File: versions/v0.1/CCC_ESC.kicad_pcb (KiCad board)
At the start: 4 copper layers, 100 x 65 mm, 158 parts, among them J1 Conn_01x04, J2 Conn_01x06, J3 Conn_01x06, J4 Conn_01x06, U1 NCP5183, U2 NCP5183, U3 NCP5183, U4 NCS20074D, U5 STM32F401CCU6_Balckpill, U6 PQDE6W-Q110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

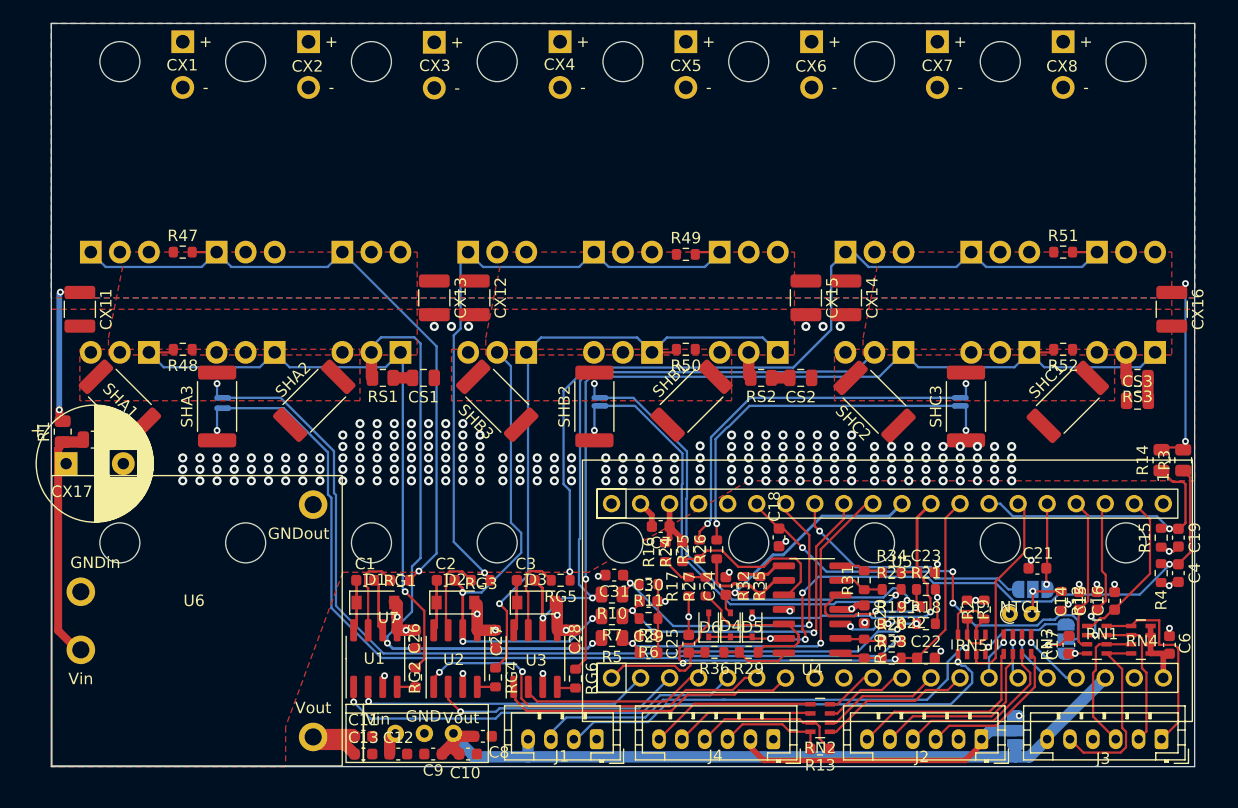
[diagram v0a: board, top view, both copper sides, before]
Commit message: finished power and gnd planes and pours
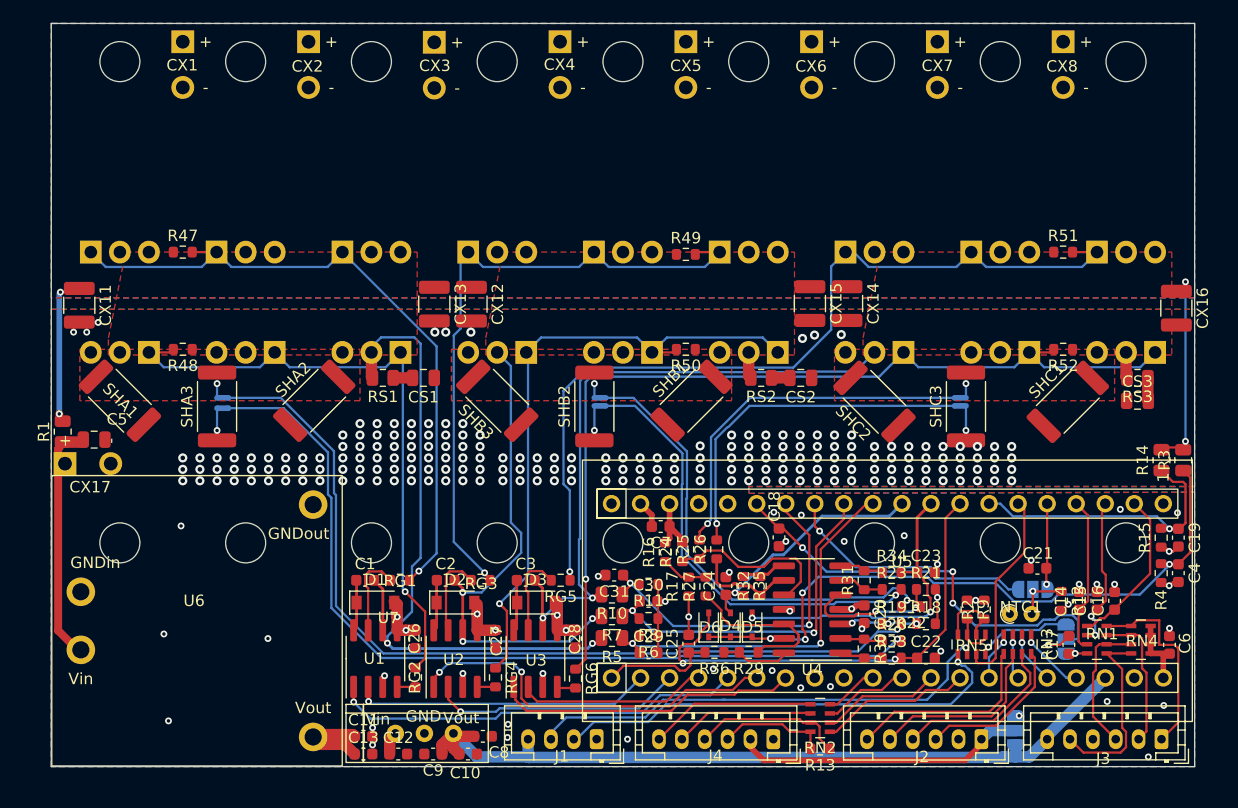
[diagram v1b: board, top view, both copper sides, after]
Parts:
- CX17: footprint Capacitor_THT:CP_Radial_D10.0mm_P5.00mm -> CCC_ESC_Custom_parts:CAP_Polaryzed
- moved CX15 0.61 mm to (116.3, 74.5)
- moved CX12 0.60 mm to (86.8, 74.5)
- moved CX13 0.55 mm to (83.5, 74.5)
- moved CX14 0.51 mm to (119.6, 74.5)
- moved CX16 0.41 mm to (148.4, 74.9)
- moved CX11 0.35 mm to (52.5, 74.7)
- moved CX17 0.10 mm to (51.2, 88.5), turned to 90 degrees
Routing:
- net V3V3: track 67.0 -> 18.5 mm
- net GND: vias 219 -> 244
- added copper zone on B.Cu, net GND
- added copper zone on In2.Cu, net GND

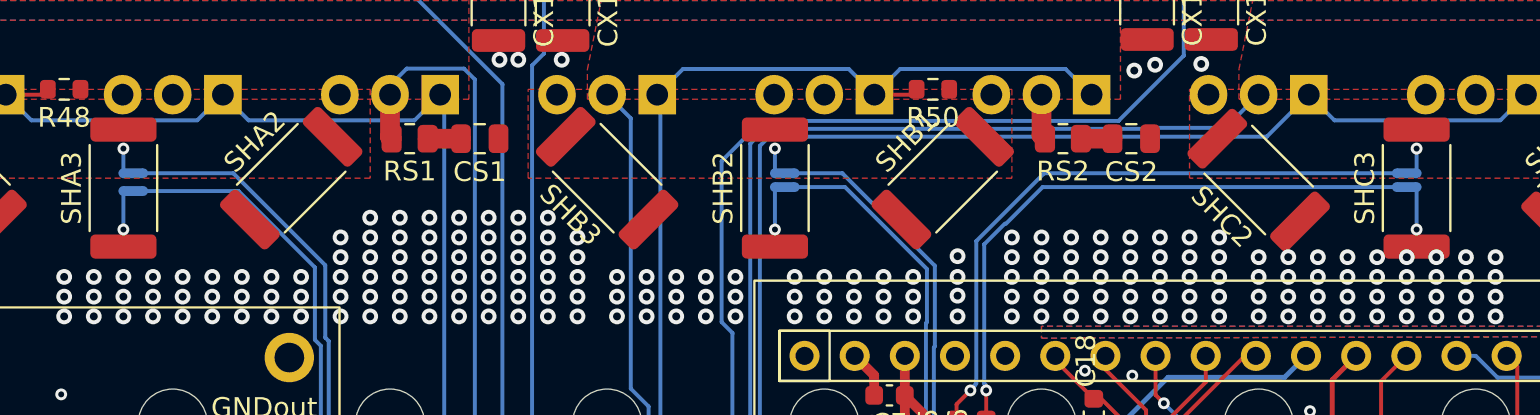
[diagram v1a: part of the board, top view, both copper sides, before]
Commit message: improved nettie gnd to not touch other gnds
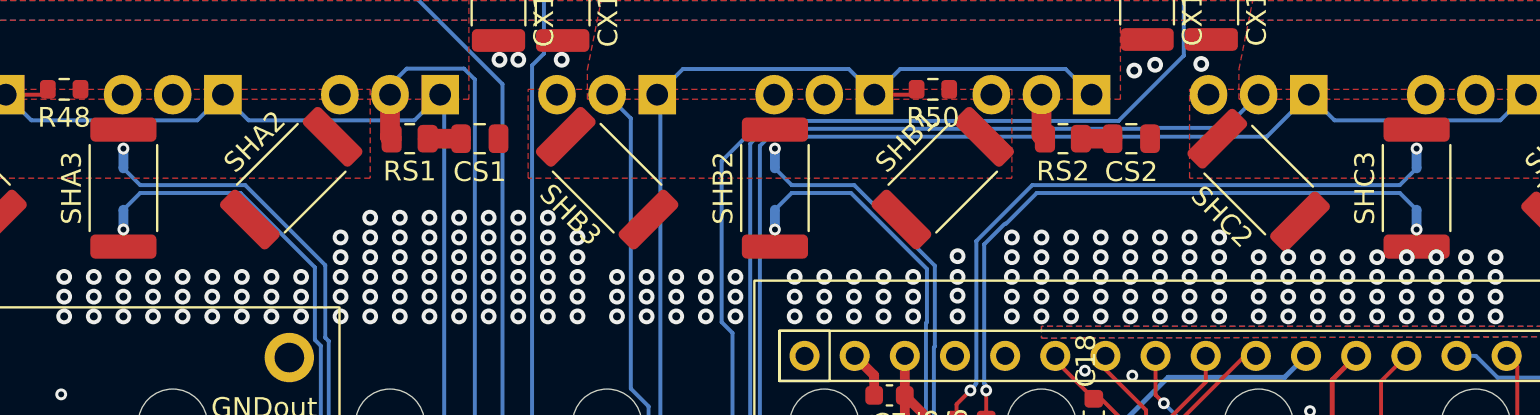
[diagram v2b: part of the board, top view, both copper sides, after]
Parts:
- moved NT4 1.72 mm to (97.5, 85.1), turned to 90 degrees
- moved NT6 1.72 mm to (130.0, 85.1), turned to 90 degrees
- moved NT2 1.53 mm to (64.5, 85.1), turned to 90 degrees
- moved NT1 0.90 mm to (64.5, 82.0), turned to -90 degrees
- moved NT3 0.90 mm to (97.5, 82.0), turned to -90 degrees
- moved NT5 0.90 mm to (130.0, 82.0), turned to -90 degrees
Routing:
- net GND: track 29.1 -> 22.8 mm
- net A_SHA_V-: track 76.4 -> 77.7 mm
- net Net-(NT3-Pad1): track 1.25 -> 0.00 mm
- net Net-(NT5-Pad1): track 1.25 -> 0.00 mm
- net Net-(NT1-Pad1): track 1.25 -> 0.00 mm
- net A_SHB_V-: track 38.9 -> 40.1 mm
- net A_SHC_V-: track 31.1 -> 32.4 mm
- net A_SHC_V+: track 32.3 -> 33.4 mm
- net A_SHB_V+: track 40.8 -> 41.9 mm
- net A_SHA_V+: track 77.1 -> 78.2 mm

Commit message: added power switch
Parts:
- added SW1: Conn_01x02, Resistor_THT:R_Axial_DIN0204_L3.6mm_D1.6mm_P1.90mm_Vertical, F.Cu at (50.9, 83.4)
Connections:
- R1 pad 2: VBAT -> Net-(R1-Pad2)
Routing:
- net VBAT: track 28.9 -> 26.6 mm, vias 4 -> 3
- net Net-(R1-Pad2): track 0.00 -> 1.42 mm
- net GND: vias 244 -> 246
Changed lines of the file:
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@@
   (net 103 "Net-(R2-Pad1)")
   (net 104 "Net-(R27-Pad1)")
+  (net 105 "Net-(R1-Pad2)")
   (footprint "Capacitor_SMD:C_0603_1608Metric" (layer "F.Cu")
     (at 103.3 94 180)
@@
     )
   )
+  (footprint "Resistor_THT:R_Axial_DIN0204_L3.6mm_D1.6mm_P1.90mm_Vertical" (layer "F.Cu")
+    (at 50.9 83.405 90)
+    (descr "Resistor, Axial_DIN0204 series, Axial, Vertical, pin pitch=1.9mm, 0.167W, length*diameter=3.6*1.6mm^2, http://cdn-reichelt.de/documents/datenblatt/B400/1_4W%23YAG.pdf")
+    (tags "Resistor Axial_DIN0204 series Axial Vertical pin pitch 1.9mm 0.167W length 3.6mm diameter 1.6mm")
+    (property "Sheetfile" "CCC_ESC.kicad_sch")
+    (property "Sheetname" "")
+    (attr through_hole)
+    (fp_text reference "SW1" (at 1.105 -2.35 90) (layer "F.SilkS")
+      (effects (font (size 1 1) (thickness 0.15)))
+    )
+    (fp_text value "Conn_01x02" (at 0.95 1.92 90) (layer "F.Fab")
+      (effects (font (size 1 1) (thickness 0.15)))
+    )
+    (fp_text user "${REFERENCE}" (at 0.95 -1.92 90) (layer "F.Fab")
+      (effects (font (size 1 1) (thickness 0.15)))
+    )
+    (fp_arc (start 0.320095 0.749359) (mid -0.813042 -0.054435) (end 0.417133 -0.7) (layer "F.SilkS") (width 0.12))
+    (fp_line (start 2.86 1.05) (end 2.86 -1.05) (layer "F.CrtYd") (width 0.05))
+    (fp_line (start -1.05 1.05) (end 2.86 1.05) (layer "F.CrtYd") (width 0.05))
+    (fp_line (start 2.86 -1.05) (end -1.05 -1.05) (layer "F.CrtYd") (width 0.05))
+    (fp_line (start -1.05 -1.05) (end -1.05 1.05) (layer "F.CrtYd") (width 0.05))
+    (fp_line (start 0 0) (end 1.9 0) (layer "F.Fab") (width 0.1))
+    (fp_circle (center 0 0) (end 0.8 0) (layer "F.Fab") (width 0.1) (fill none))
+    (pad "1" thru_hole circle (at 0 0 90) (size 1.4 1.4) (drill 0.7) (layers *.Cu *.Mask)
+      (net 105 "Net-(R1-Pad2)") (pinfunction "Pin_1") (pintype "passive"))
+    (pad "2" thru_hole oval (at 1.9 0 90) (size 1.4 1.4) (drill 0.7) (layers *.Cu *.Mask)
+      (net 17 "VBAT") (pinfunction "Pin_2") (pintype "passive"))
+    (model "${KICAD6_3DMODEL_DIR}/Resistor_THT.3dshapes/R_Axial_DIN0204_L3.6mm_D1.6mm_P1.90mm_Vertical.wrl"
+      (offset (xyz 0 0 0))
+      (scale (xyz 1 1 1))
+      (rotate (xyz 0 0 0))
+    )
+  )
   (footprint "Resistor_SMD:R_0603_1608Metric" (layer "F.Cu")
     (at 131.6 101.2625 90)
@@
       (net 6 "Net-(C5-Pad1)") (pintype "passive"))
     (pad "2" smd roundrect (at 0.9125 0 90) (size 1.025 1.4) (layers "F.Cu" "F.Paste" "F.Mask") (roundrect_rratio 0.243902)
-      (net 17 "VBAT") (pintype "passive"))
+      (net 105 "Net-(R1-Pad2)") (pintype "passive"))
     (model "${KICAD6_3DMODEL_DIR}/Resistor_SMD.3dshapes/R_0805_2012Metric.wrl"
       (offset (xyz 0 0 0))
@@
   (via (at 101.5 89) (size 0.8) (drill 0.4) (layers "F.Cu" "B.Cu") (free) (net 9))
   (via (at 86 87) (size 0.8) (drill 0.4) (layers "F.Cu" "B.Cu") (free) (net 9))
+  (via (at 51.55 78.3) (size 0.6) (drill 0.3) (layers "F.Cu" "B.Cu") (net 9))
   (via (at 104.5 88) (size 0.8) (drill 0.4) (layers "F.Cu" "B.Cu") (free) (net 9))
   (via (at 125 89) (size 0.8) (drill 0.4) (layers "F.Cu" "B.Cu") (free) (net 9))
@@
   (via (at 104.5 90) (size 0.8) (drill 0.4) (layers "F.Cu" "B.Cu") (free) (net 9))
   (via (at 112.5 86) (size 0.8) (drill 0.4) (layers "F.Cu" "B.Cu") (free) (net 9))
+  (via (at 54.1 77) (size 0.6) (drill 0.3) (layers "F.Cu" "B.Cu") (net 9))
   (via (at 80 90) (size 0.8) (drill 0.4) (layers "F.Cu" "B.Cu") (free) (net 9))
   (via (at 77 90) (size 0.8) (drill 0.4) (layers "F.Cu" "B.Cu") (free) (net 9))
@@
   (segment (start 149 87.0875) (end 147.1 87.0875) (width 0.2) (layer "F.Cu") (net 17))
   (segment (start 149.2 86.55) (end 149.2 86.8875) (width 0.2) (layer "F.Cu") (net 17))
-  (segment (start 50.7 84.15) (end 50.7 84.2) (width 0.7) (layer "F.Cu") (net 17))
   (via (at 149.2 86.55) (size 0.6) (drill 0.3) (layers "F.Cu" "B.Cu") (net 17))
-  (via (at 50.7 84.15) (size 0.6) (drill 0.3) (layers "F.Cu" "B.Cu") (net 17))
   (via (at 50.8 73.5) (size 0.6) (drill 0.3) (layers "F.Cu" "B.Cu") (net 17))
   (via (at 149.2 72.6) (size 0.6) (drill 0.3) (layers "F.Cu" "B.Cu") (net 17))
+  (segment (start 50.5 73.85) (end 50.5 81.105) (width 0.3) (layer "B.Cu") (net 17))
+  (segment (start 50.8 73.5) (end 50.8 73.55) (width 0.2) (layer "B.Cu") (net 17))
+  (segment (start 50.8 73.55) (end 50.5 73.85) (width 0.3) (layer "B.Cu") (net 17))
   (segment (start 50.7 73.6) (end 50.8 73.5) (width 0.2) (layer "B.Cu") (net 17))
-  (segment (start 50.7 84.15) (end 50.7 73.6) (width 0.5) (layer "B.Cu") (net 17))
+  (segment (start 50.5 81.105) (end 50.9 81.505) (width 0.3) (layer "B.Cu") (net 17))
   (segment (start 149.2 72.6) (end 149.2 86.55) (width 0.2) (layer "B.Cu") (net 17))
   (segment (start 78.985 103.785) (end 78.985 103.075) (width 0.25) (layer "F.Cu") (net 18))
@@
   (segment (start 115.35 103.7) (end 115.354507 103.695493) (width 0.2) (layer "F.Cu") (net 104))
   (segment (start 108.600481 101.300481) (end 107.325 100.025) (width 0.2) (layer "F.Cu") (net 104))
+  (segment (start 50.9 84.6875) (end 51 84.7875) (width 0.2) (layer "F.Cu") (net 105))
+  (segment (start 50.9 83.405) (end 50.9 84.6875) (width 0.5) (layer "F.Cu") (net 105))
   (zone (net 18) (net_name "PHASE_A") (layer "F.Cu") (hatch edge 0.508)
     (priority 3)

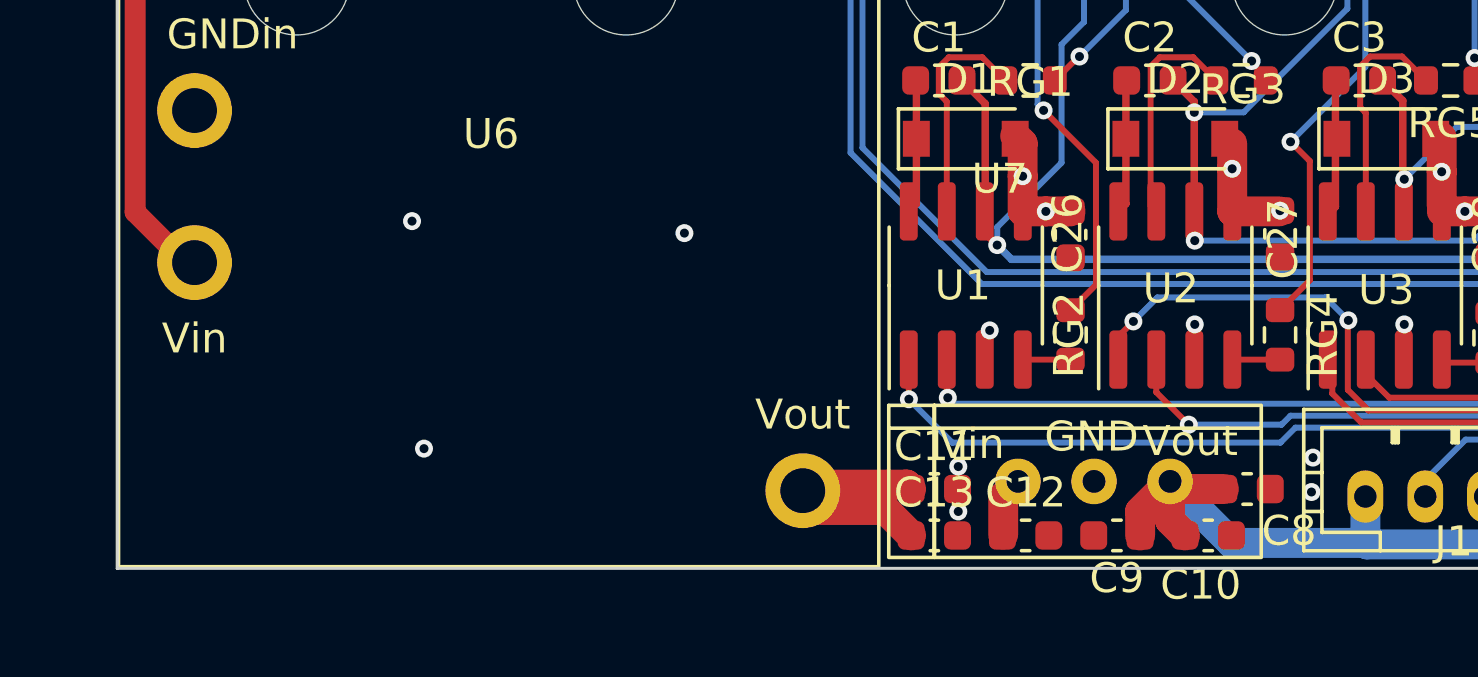
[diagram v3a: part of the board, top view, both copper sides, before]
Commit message: second dcdc footprint and improved to220 replacement footprint
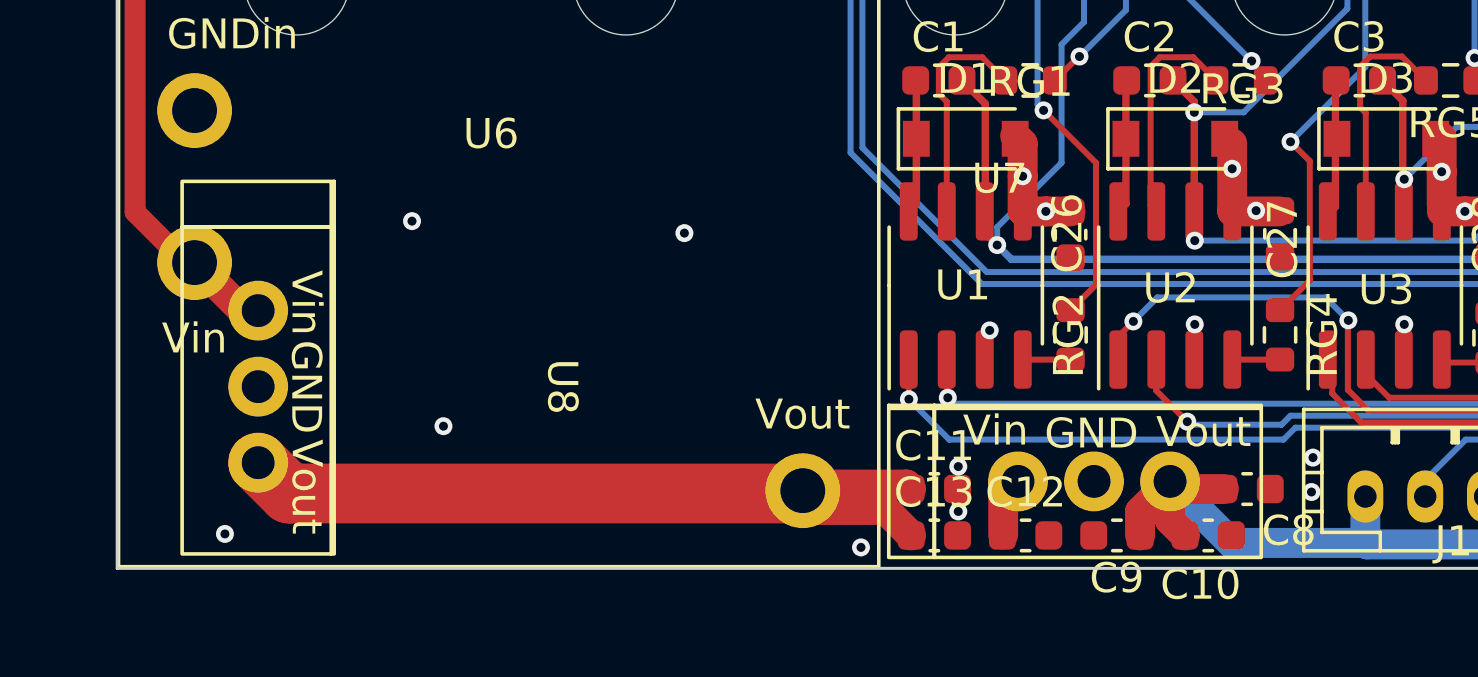
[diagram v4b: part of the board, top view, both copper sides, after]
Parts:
- added U8: TO220_replacement_module, CCC_ESC_Custom_parts:TO220_replacement_module, F.Cu at (57.2, 103.8)
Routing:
- net V12V: track 23.4 -> 42.8 mm
- net Net-(C5-Pad1): track 21.0 -> 24.1 mm
- net GND: vias 246 -> 248
